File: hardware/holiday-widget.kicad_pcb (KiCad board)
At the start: 4 copper layers, 108.4 x 65.8 mm, 155 parts, among them J2 UART, J33 Conn_ARM_JTAG_SWD_10, J4 BATTERY POWER, J5 VDC POWER, J7 Speaker, Q1 MMBT3906, Q10 MMBT3906, Q11 MMBT3906, Q12 MMBT3906, Q18 MMBT3906, Q19 MMBT3906, Q2 MMBT3906, Q3 MMBT3906, Q4 MMBT3906, Q5 MMBT3906, Q6 MMBT3906, Q7 MMBT3906, Q8 MMBT3906, Q9 MMBT3906, SW1 SW_Push, SW4 SW_Push, U1 STM32L072RBTx, U2 TPS61200DRC, U4 IMP23ABSU, U5 LSM6DSM, U6 VCNL_4020, U7 PAM8302AAD, U8 OPA504

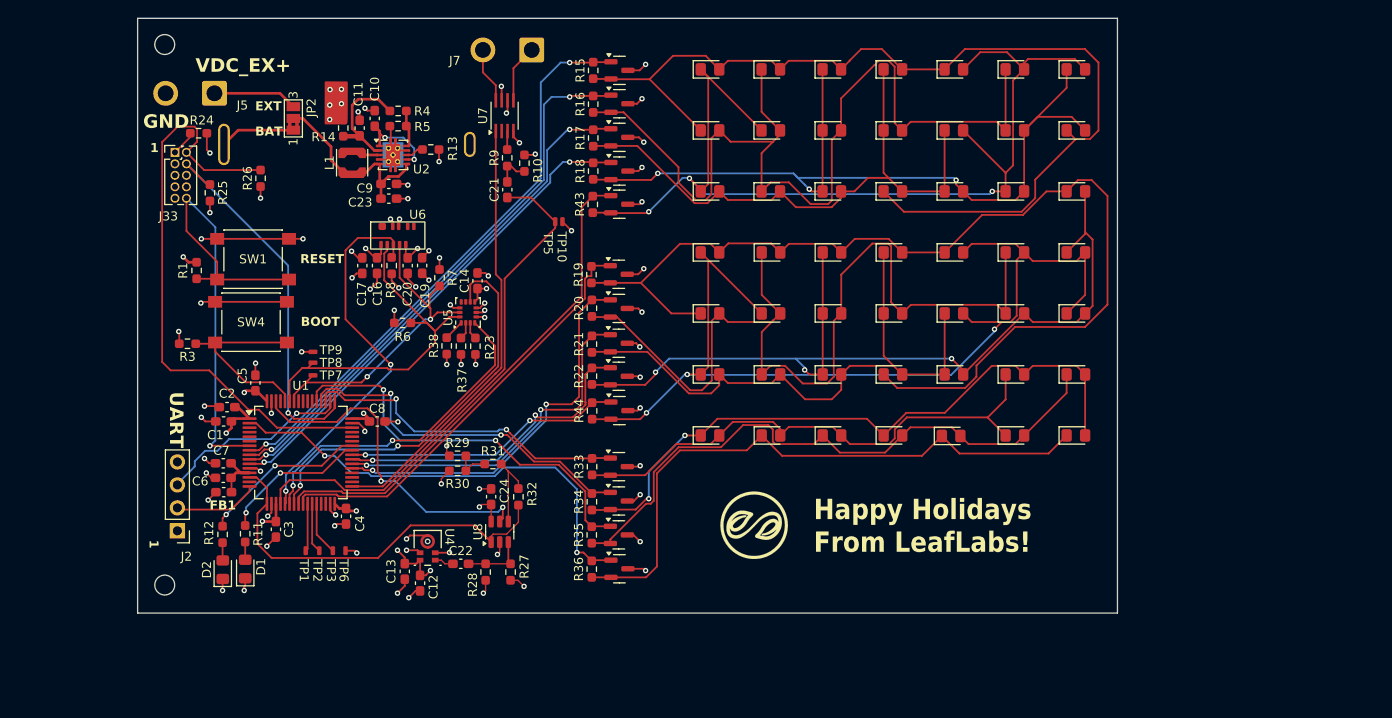
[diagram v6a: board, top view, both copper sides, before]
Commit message: Neaten up the layout of the LED array
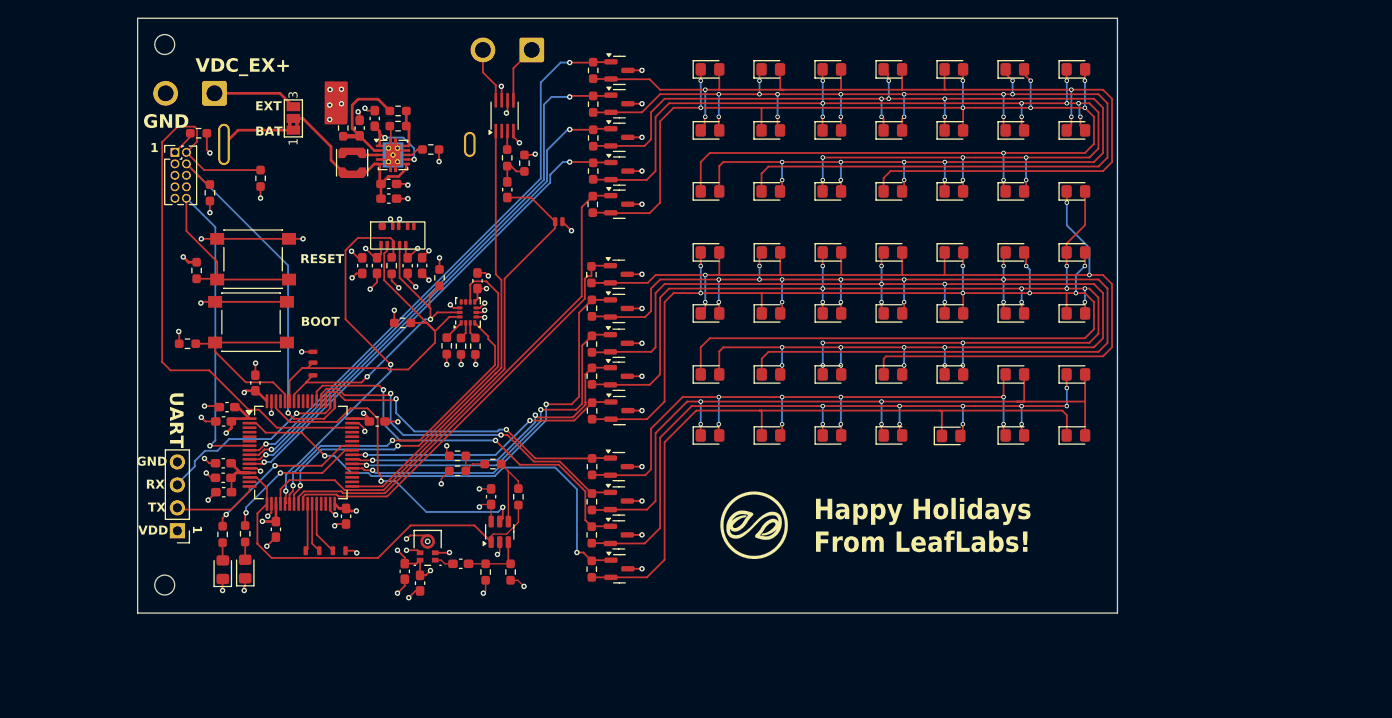
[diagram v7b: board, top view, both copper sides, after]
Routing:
- net /Input and Output/LED Output/CTRL2: track 64.9 -> 134.7 mm, vias 0 -> 14
- net /Input and Output/LED Output1/CTRL2: track 67.1 -> 135.3 mm, vias 0 -> 13
- net /Input and Output/LED Output1/CTRL3: track 95.2 -> 131.3 mm, vias 3 -> 13
- net /Input and Output/LED Output/CTRL3: track 90.5 -> 125.8 mm, vias 3 -> 15
- net /Input and Output/LED Output1/CTRL4: track 111.6 -> 143.7 mm, vias 3 -> 8
- net /Input and Output/LED Output/CTRL4: track 111.3 -> 142.4 mm, vias 3 -> 10
- net /Input and Output/LED Output1/CTRL1: track 101.6 -> 131.0 mm, vias 0 -> 13
- net /Input and Output/LED Output/CTRL1: track 102.9 -> 129.8 mm, vias 0 -> 14
- net /Input and Output/LED Output2/CTRL0: track 58.6 -> 70.5 mm, vias 0 -> 8
- net /Input and Output/LED Output2/CTRL2: track 69.2 -> 80.4 mm, vias 0 -> 10
- net /Input and Output/LED Output2/CTRL1: track 72.4 -> 81.6 mm, vias 2 -> 4
- net /Input and Output/LED Output2/CTRL3: track 68.6 -> 76.1 mm
- net /Input and Output/LED Output/CTRL0: track 109.2 -> 113.2 mm, vias 0 -> 4
- net /Input and Output/LED Output1/CTRL0: track 116.1 -> 120.2 mm, vias 0 -> 4
- net /GND: track 109.3 -> 105.5 mm
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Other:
- board text added: "Holiday Widget v2.1"
- board text added: "RX"
- board text added: "TX"
- board text added: "VDD"
- board text removed: "Holiday Widget v2.0"

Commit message: Change many passives to 0402 and assign part numbers
Incorporate 0402 parts where possible
Assign Manufacturer Part Numbers to parts where possible
Update layout for the new passive sizes
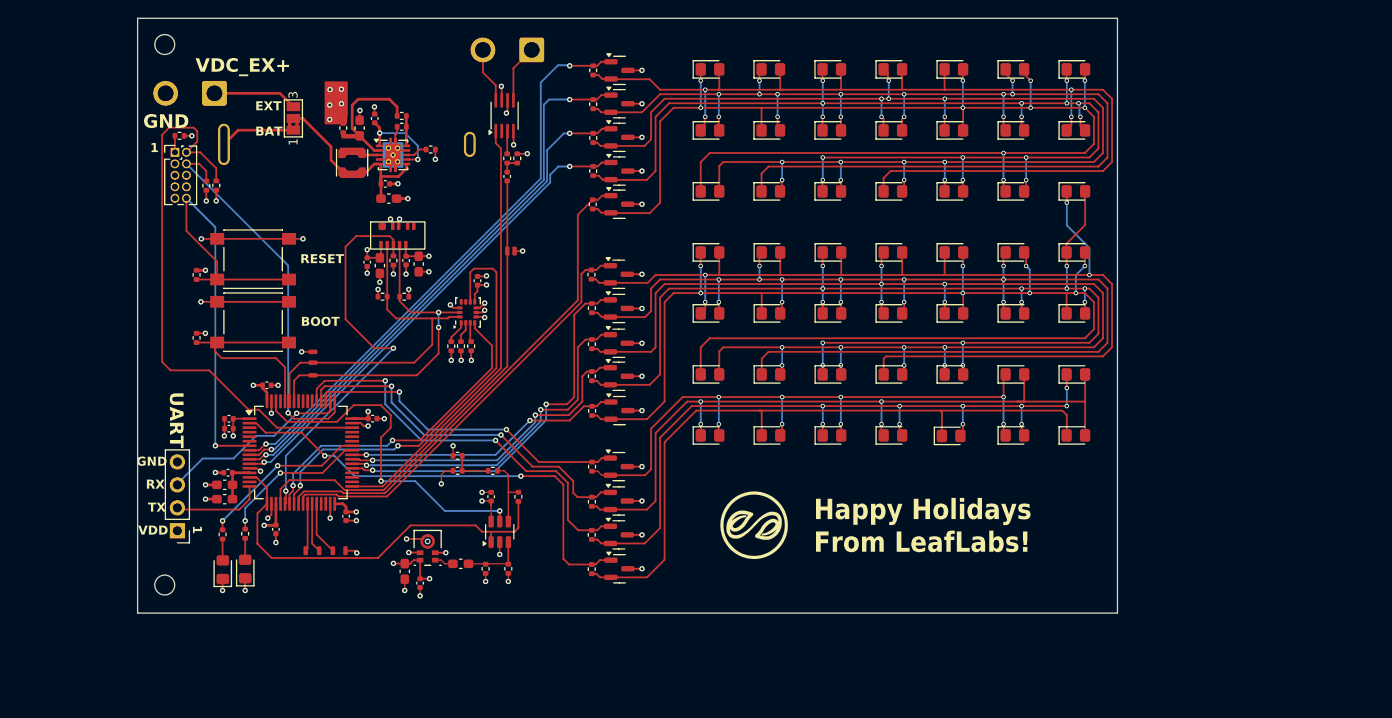
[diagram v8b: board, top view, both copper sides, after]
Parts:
- C1, C10, C12, C14, C17, C2, C20, C21, C24, C3, C4, C5, C7, C8, C9: footprint Capacitor_SMD:C_0603_1608Metric_Pad1.08x0.95mm_HandSolder -> Capacitor_SMD:C_0402_1005Metric
- R1, R10, R11, R12, R13, R14, R15, R16, R17, R18, R19, R20, R21, R22, R23, R24, R25, R26, R27, R28, R29, R3, R30, R31, R32, R33, R34, R35, R36, R37, R38, R4, R43, R44, R5, R6, R7, R8, R9: footprint Resistor_SMD:R_0603_1608Metric_Pad0.98x0.95mm_HandSolder -> Resistor_SMD:R_0402_1005Metric
- moved TP5 6.22 mm to (168.1, 96.8)
- moved TP10 6.22 mm to (168.9, 96.8)
- moved R26 4.96 mm to (135.9, 89.6)
- moved R7 4.43 mm to (156.7, 101.9), turned to 180 degrees
- moved R6 3.65 mm to (154.3, 101.9)
- moved R24 2.13 mm to (131.8, 84.1)
- moved C21 1.46 mm to (168.1, 88.6)
- moved C2 1.30 mm to (137.3, 115.4)
- moved C5 1.30 mm to (141.5, 111.7), turned to 0 degrees
- moved R3 1.20 mm to (133.7, 106.5), turned to 90 degrees
- moved C7 1.18 mm to (137.2, 121.4)
- moved C1 0.99 mm to (137.3, 116.5)
- moved R10 0.95 mm to (169.2, 86.6)
- moved R25 0.88 mm to (134.8, 89.6)
- moved C6 0.79 mm to (136.8, 122.7)
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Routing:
- net /GND: track 105.5 -> 94.6 mm, vias 65 -> 64
- net /VDD: track 64.2 -> 58.9 mm, vias 31 -> 29
- net /Input and Output/AUDIO_OUT: track 57.9 -> 53.5 mm
- net /mcu/SWDIO: track 65.1 -> 61.8 mm
- net /Sensors/IMU_INT2: track 44.4 -> 47.4 mm
- net /I2C.SDA: track 41.3 -> 39.2 mm
- net /mcu/BOOT: track 21.4 -> 23.4 mm
- net /Sensors/VCNL4020_INT: track 42.7 -> 44.5 mm
- net Net-(C21-Pad2): track 3.89 -> 2.16 mm
- net Net-(U2-VOUT): track 13.4 -> 15.0 mm
- net /mcu/VDDA: track 6.29 -> 4.82 mm
- net Net-(U8--): track 9.13 -> 7.69 mm
- net /Power/VAUX: track 8.73 -> 10.1 mm
- net /Audio Amp/AUDIO_AMP_EN: track 37.6 -> 38.9 mm
- net Net-(J33-VTref): track 2.82 -> 1.83 mm
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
